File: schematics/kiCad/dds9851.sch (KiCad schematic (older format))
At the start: 8 parts, among them J1 PJ-102A, U1 Teensy-LC, U2 HC06

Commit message: new schematic
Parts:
- removed J1: PJ-102A, dmcginnis427:DC21Jack, symbol blinky-lite-basic-rescue:PJ-102A-dk_Barrel-Power-Connectors
- added TP-5V1, TP-GND1: TestPoint, Connector_PinHeader_2.54mm:PinHeader_1x01_P2.54mm_Vertical, symbol Connector:TestPoint
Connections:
- wire segments 31 -> 26
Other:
- moved on the sheet: C1
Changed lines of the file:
@@
 EESchema Schematic File Version 4
-LIBS:blinky-lite-basic-cache
 EELAYER 30 0
 EELAYER END
@@
 L power:GND #PWR010
 U 1 1 5E09DD5B
-P 10150 2100
-F 0 "#PWR010" H 10150 1850 50  0001 C CNN
-F 1 "GND" V 10155 1972 50  0000 R CNN
-F 2 "" H 10150 2100 50  0001 C CNN
-F 3 "" H 10150 2100 50  0001 C CNN
-	1    10150 2100
+P 10300 2200
+F 0 "#PWR010" H 10300 1950 50  0001 C CNN
+F 1 "GND" V 10305 2072 50  0000 R CNN
+F 2 "" H 10300 2200 50  0001 C CNN
+F 3 "" H 10300 2200 50  0001 C CNN
+	1    10300 2200
 	0    -1   -1   0
 $EndComp
@@
 L power:PWR_FLAG #FLG03
 U 1 1 5E13850E
-P 10000 2200
-F 0 "#FLG03" H 10000 2275 50  0001 C CNN
-F 1 "PWR_FLAG" H 10000 2373 50  0000 C CNN
-F 2 "" H 10000 2200 50  0001 C CNN
-F 3 "~" H 10000 2200 50  0001 C CNN
-	1    10000 2200
-	-1   0    0    1
-$EndComp
-Wire Wire Line
-	10000 2200 10000 2100
-Wire Wire Line
-	10000 2100 10150 2100
+P 9450 2300
+F 0 "#FLG03" H 9450 2375 50  0001 C CNN
+F 1 "PWR_FLAG" H 9450 2473 50  0000 C CNN
+F 2 "" H 9450 2300 50  0001 C CNN
+F 3 "~" H 9450 2300 50  0001 C CNN
+	1    9450 2300
+	-1   0    0    1
+$EndComp
+Wire Wire Line
+	9450 2300 9450 2200
 Wire Wire Line
 	10000 1800 10000 1900
 Wire Wire Line
 	10000 1900 10200 1900
-Connection ~ 10000 1900
-Connection ~ 10000 2100
 Wire Wire Line
 	10200 1250 10200 1900
@@
 L Device:C C1
 U 1 1 5E0B2B99
-P 9600 1350
-F 0 "C1" V 9348 1350 50  0000 C CNN
-F 1 "1uF" V 9439 1350 50  0000 C CNN
-F 2 "Capacitor_SMD:C_1206_3216Metric_Pad1.42x1.75mm_HandSolder" H 9638 1200 50  0001 C CNN
-F 3 "~" H 9600 1350 50  0001 C CNN
-	1    9600 1350
-	0    1    1    0
-$EndComp
-Wire Wire Line
-	9450 1350 9450 1900
-Wire Wire Line
-	9450 1900 10000 1900
-Wire Wire Line
-	9750 1350 9750 2100
-Wire Wire Line
-	9750 2100 10000 2100
+P 9450 2050
+F 0 "C1" V 9198 2050 50  0000 C CNN
+F 1 "1uF" V 9289 2050 50  0000 C CNN
+F 2 "Capacitor_SMD:C_1206_3216Metric_Pad1.42x1.75mm_HandSolder" H 9488 1900 50  0001 C CNN
+F 3 "~" H 9450 2050 50  0001 C CNN
+	1    9450 2050
+	-1   0    0    1
+$EndComp
 $Comp
 L power:GND #PWR017
@@
 NoConn ~ 6800 4050
 NoConn ~ 6800 4150
-NoConn ~ 4450 4250
 NoConn ~ 4450 4150
 NoConn ~ 4450 4050
@@
 Wire Wire Line
 	4000 2350 3800 2350
-Wire Wire Line
-	4050 2650 4450 2650
-$Comp
-L blinky-lite-basic-rescue:PJ-102A-dk_Barrel-Power-Connectors J1
-U 1 1 5E3829F9
-P 9450 850
-F 0 "J1" V 9337 606 50  0000 R CNN
-F 1 "PJ-102A" V 9428 606 50  0000 R CNN
-F 2 "dmcginnis427:DC21Jack" H 9650 1050 60  0001 L CNN
-F 3 "" H 9650 1150 60  0001 L CNN
-F 4 "" H 9650 1250 60  0001 L CNN "Digi-Key_PN"
-F 5 "" H 9650 1350 60  0001 L CNN "MPN"
-F 6 "" H 9650 1450 60  0001 L CNN "Category"
-F 7 "" H 9650 1550 60  0001 L CNN "Family"
-F 8 "" H 9650 1650 60  0001 L CNN "DK_Datasheet_Link"
-F 9 "" H 9650 1750 60  0001 L CNN "DK_Detail_Page"
-F 10 "" H 9650 1850 60  0001 L CNN "Description"
-F 11 "" H 9650 1950 60  0001 L CNN "Manufacturer"
-F 12 "" H 9650 2050 60  0001 L CNN "Status"
-	1    9450 850
-	0    -1   1    0
-$EndComp
-Wire Wire Line
-	9450 950  9450 1350
-Connection ~ 9450 1350
-Wire Wire Line
-	9650 950  9750 950
-Wire Wire Line
-	9750 950  9750 1350
-Connection ~ 9750 1350
-Wire Wire Line
-	9550 950  9650 950
-Connection ~ 9650 950
 $Comp
 L teensy:Teensy-LC U1
@@
 	1    0    0    -1
 $EndComp
-Wire Wire Line
-	4050 3150 4050 2650
-Wire Wire Line
-	3450 3150 4050 3150
-Wire Wire Line
-	3150 3150 3100 3150
-Wire Wire Line
-	2800 3150 2700 3150
-$Comp
-L Device:LED D2
-U 1 1 5E10E10F
-P 3300 3150
-F 0 "D2" H 3293 2895 50  0000 C CNN
-F 1 "LED" H 3293 2986 50  0000 C CNN
-F 2 "LED_THT:LED_D5.0mm" H 3300 3150 50  0001 C CNN
-F 3 "~" H 3300 3150 50  0001 C CNN
-	1    3300 3150
-	1    0    0    -1
-$EndComp
-$Comp
-L Device:R R2
-U 1 1 5E10E0FC
-P 2950 3150
-F 0 "R2" V 2743 3150 50  0000 C CNN
-F 1 "220" V 2834 3150 50  0000 C CNN
-F 2 "Resistor_SMD:R_1206_3216Metric_Pad1.42x1.75mm_HandSolder" V 2880 3150 50  0001 C CNN
-F 3 "~" H 2950 3150 50  0001 C CNN
-	1    2950 3150
-	0    -1   -1   0
-$EndComp
-$Comp
-L power:GND #PWR013
-U 1 1 5E10E108
-P 2700 3150
-F 0 "#PWR013" H 2700 2900 50  0001 C CNN
-F 1 "GND" V 2705 3022 50  0000 R CNN
-F 2 "" H 2700 3150 50  0001 C CNN
-F 3 "" H 2700 3150 50  0001 C CNN
-	1    2700 3150
-	0    1    1    0
-$EndComp
 NoConn ~ 6800 4250
 NoConn ~ 4450 3550
@@
 NoConn ~ 4450 2850
 NoConn ~ 4450 2750
+Wire Wire Line
+	3150 4250 3100 4250
+Wire Wire Line
+	2800 4250 2700 4250
+$Comp
+L Device:LED D2
+U 1 1 5E56B921
+P 3300 4250
+F 0 "D2" H 3293 3995 50  0000 C CNN
+F 1 "LED" H 3293 4086 50  0000 C CNN
+F 2 "LED_THT:LED_D5.0mm" H 3300 4250 50  0001 C CNN
+F 3 "~" H 3300 4250 50  0001 C CNN
+	1    3300 4250
+	1    0    0    -1
+$EndComp
+$Comp
+L Device:R R2
+U 1 1 5E56B927
+P 2950 4250
+F 0 "R2" V 2743 4250 50  0000 C CNN
+F 1 "220" V 2834 4250 50  0000 C CNN
+F 2 "Resistor_SMD:R_1206_3216Metric_Pad1.42x1.75mm_HandSolder" V 2880 4250 50  0001 C CNN
+F 3 "~" H 2950 4250 50  0001 C CNN
+	1    2950 4250
+	0    -1   -1   0
+$EndComp
+$Comp
+L power:GND #PWR05
+U 1 1 5E56B92D
+P 2700 4250
+F 0 "#PWR05" H 2700 4000 50  0001 C CNN
+F 1 "GND" V 2705 4122 50  0000 R CNN
+F 2 "" H 2700 4250 50  0001 C CNN
+F 3 "" H 2700 4250 50  0001 C CNN
+	1    2700 4250
+	0    1    1    0
+$EndComp
+Wire Wire Line
+	3450 4250 4450 4250
+NoConn ~ 4450 2650
+Wire Wire Line
+	10300 2200 9450 2200
+Connection ~ 9450 2200
+Wire Wire Line
+	10000 1900 9450 1900
+Connection ~ 10000 1900
+$Comp
+L Connector:TestPoint TP-5V1
+U 1 1 5F51E042
+P 8750 1850
+F 0 "TP-5V1" H 8808 1968 50  0000 L CNN
+F 1 "TestPoint" H 8808 1877 50  0000 L CNN
+F 2 "Connector_PinHeader_2.54mm:PinHeader_1x01_P2.54mm_Vertical" H 8950 1850 50  0001 C CNN
+F 3 "~" H 8950 1850 50  0001 C CNN
+	1    8750 1850
+	1    0    0    -1
+$EndComp
+$Comp
+L Connector:TestPoint TP-GND1
+U 1 1 5F51E6D9
+P 8750 2250
+F 0 "TP-GND1" H 8692 2276 50  0000 R CNN
+F 1 "TestPoint" H 8692 2367 50  0000 R CNN
+F 2 "Connector_PinHeader_2.54mm:PinHeader_1x01_P2.54mm_Vertical" H 8950 2250 50  0001 C CNN
+F 3 "~" H 8950 2250 50  0001 C CNN
+	1    8750 2250
+	-1   0    0    1
+$EndComp
+Wire Wire Line
+	9450 2200 8750 2200
+Wire Wire Line
+	8750 2200 8750 2250
+Wire Wire Line
+	9450 1900 8750 1900
+Wire Wire Line
+	8750 1900 8750 1850
+Connection ~ 9450 1900
 $EndSCHEMATC

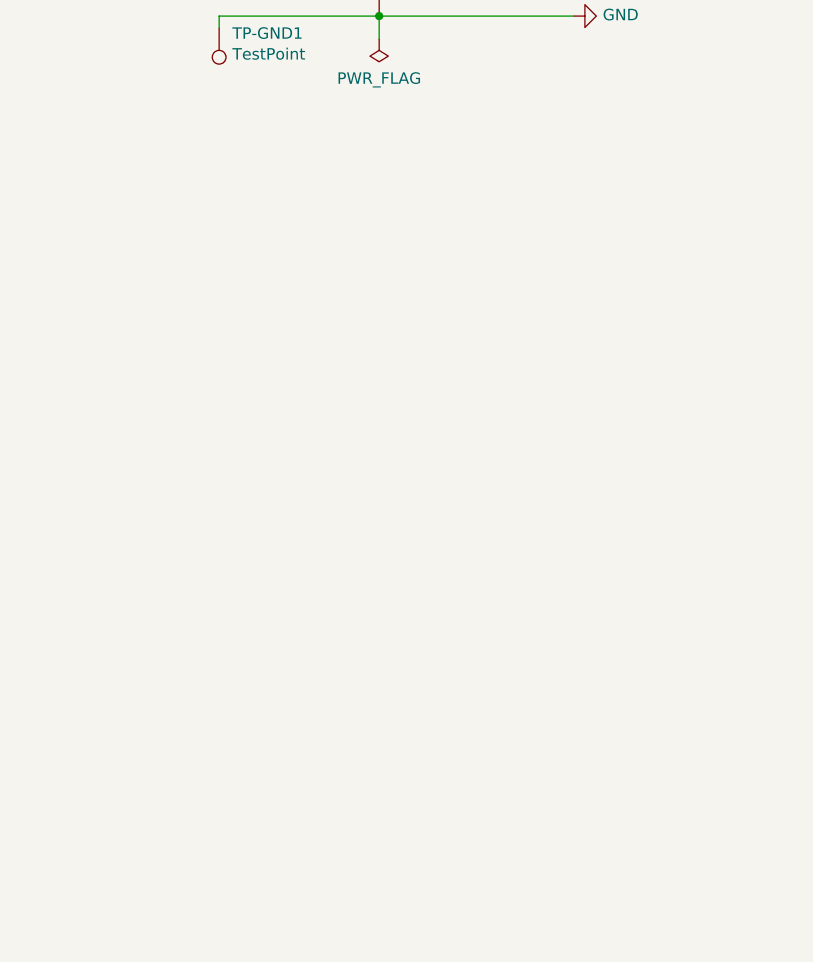
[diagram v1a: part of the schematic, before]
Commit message: added 9851 LTC, and MCP libraries
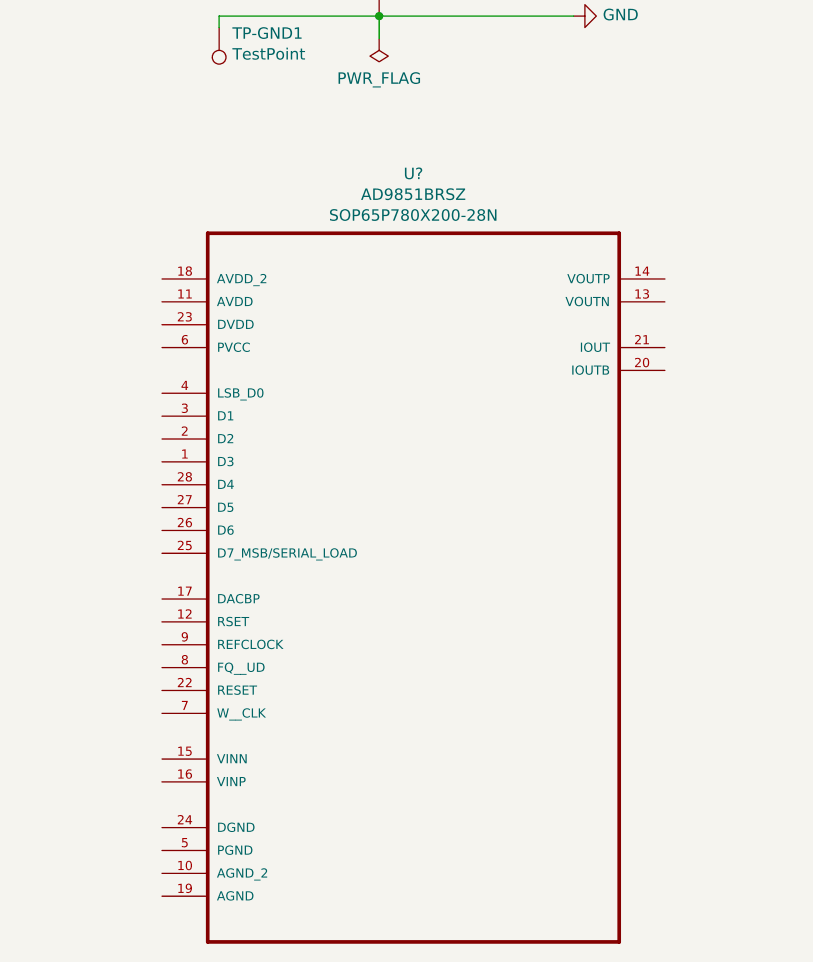
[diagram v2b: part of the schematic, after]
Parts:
- added U?: AD9851BRSZ, SOP65P780X200-28N, symbol ad9851:AD9851BRSZ
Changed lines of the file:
@@
 	8750 1900 8750 1850
 Connection ~ 9450 1900
+$Comp
+L ad9851:AD9851BRSZ U?
+U 1 1 5F7C104F
+P 9600 4550
+F 0 "U?" H 9600 6210 50  0000 C CNN
+F 1 "AD9851BRSZ" H 9600 6119 50  0000 C CNN
+F 2 "SOP65P780X200-28N" H 9600 6028 50  0000 C CNN
+F 3 "ANALOG DEVICES" H 9600 4550 50  0001 L BNN
+F 4 "-" H 9600 4550 50  0001 L BNN "Field4"
+F 5 "AD9851BRSZ" H 9600 4550 50  0001 L BNN "Field5"
+F 6 "19M8949" H 9600 4550 50  0001 L BNN "Field6"
+F 7 "SSOP-28" H 9600 4550 50  0001 L BNN "Field7"
+	1    9600 4550
+	1    0    0    -1
+$EndComp
 $EndSCHEMATC

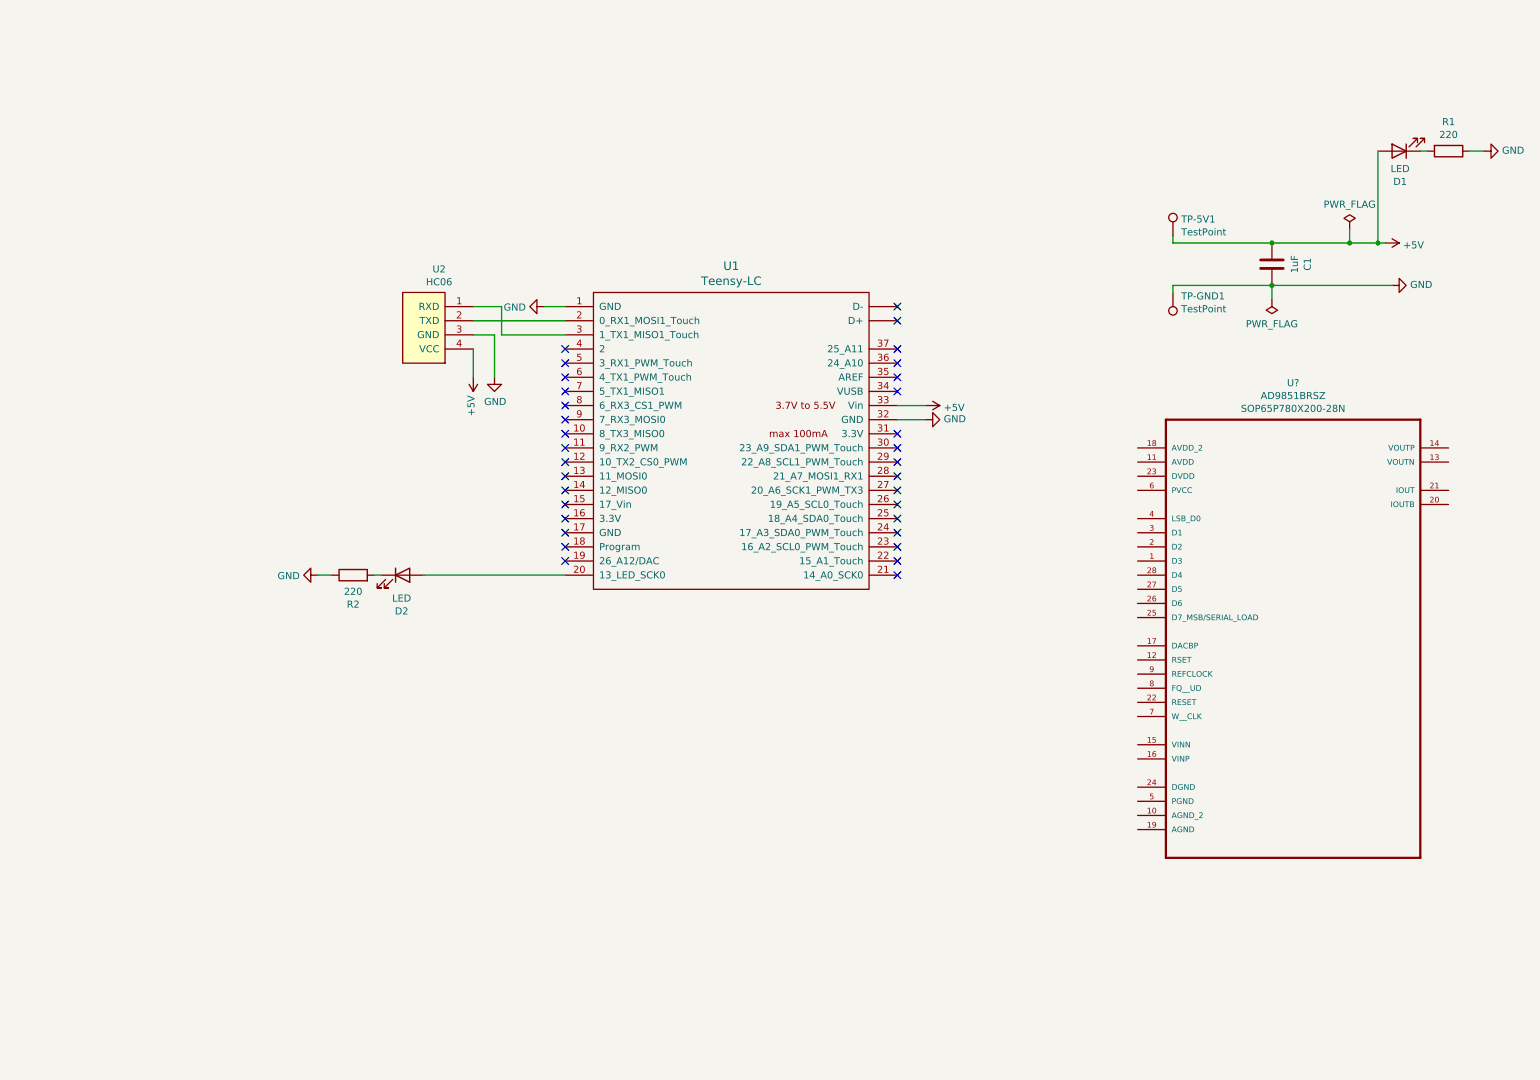
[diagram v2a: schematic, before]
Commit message: schematic done - working on pcb
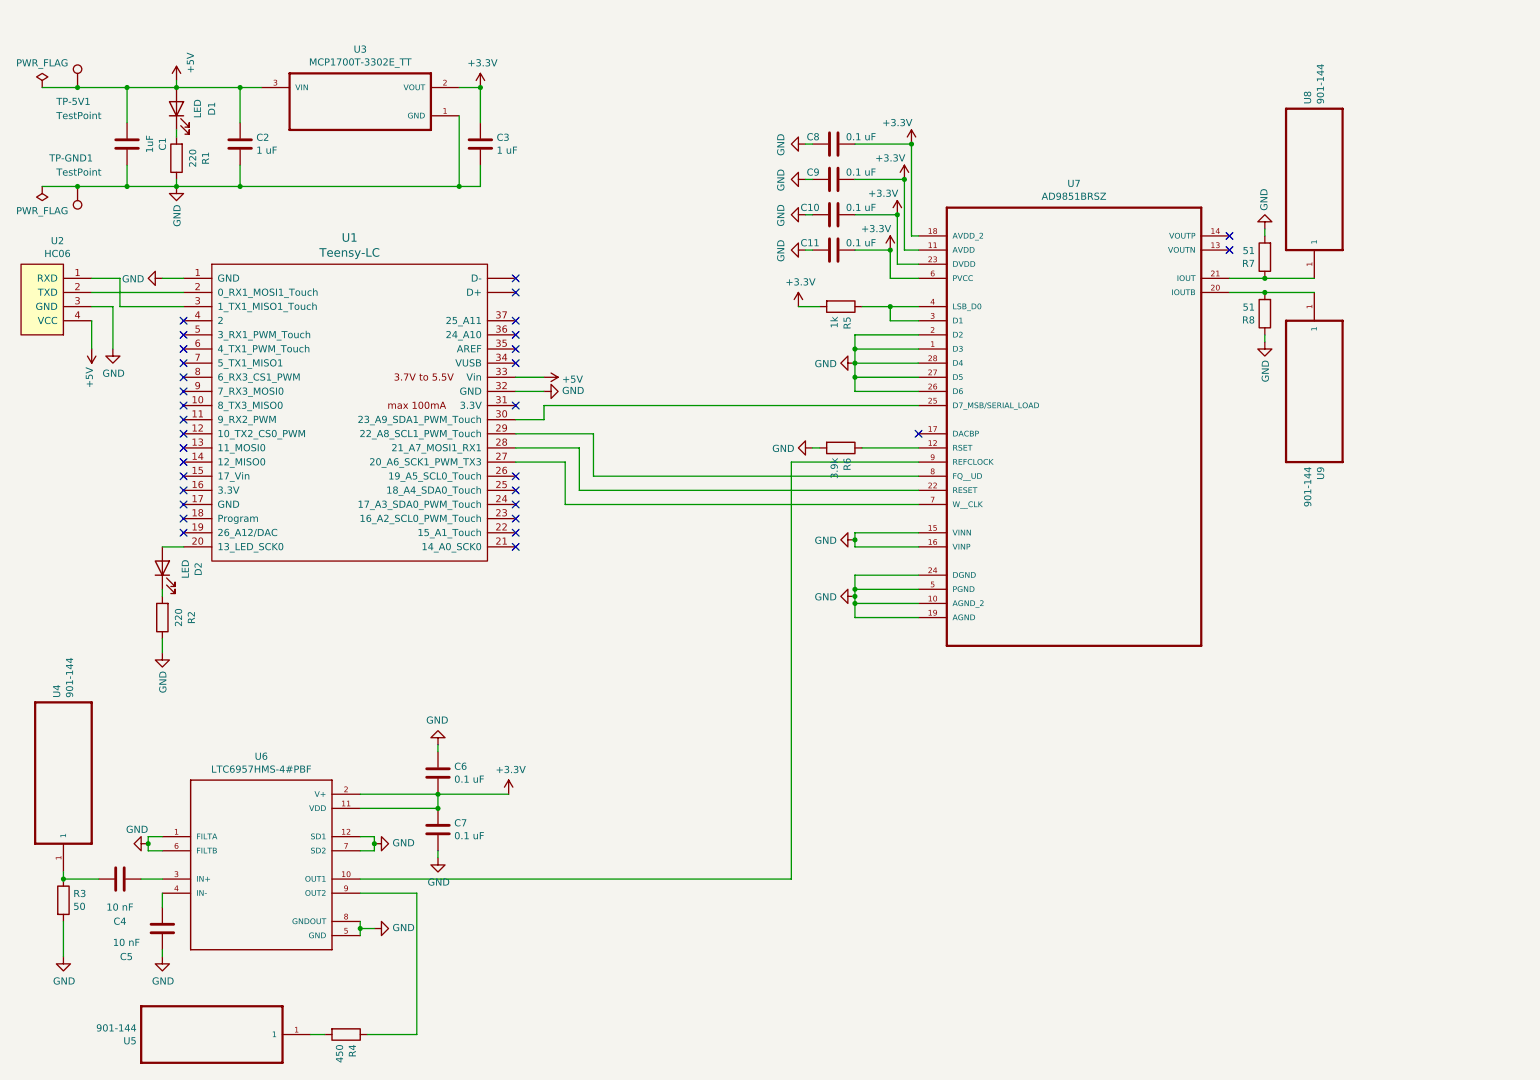
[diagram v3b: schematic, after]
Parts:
- removed U?: AD9851BRSZ, SOP65P780X200-28N, symbol ad9851:AD9851BRSZ
- added C10, C11, C6, C7, C8, C9: 0.1 uF, Capacitor_SMD:C_1206_3216Metric_Pad1.42x1.75mm_HandSolder, symbol Device:C
- added C2, C3: 1 uF, Capacitor_SMD:C_1206_3216Metric_Pad1.42x1.75mm_HandSolder, symbol Device:C
- added C4, C5: 10 nF, Capacitor_SMD:C_1206_3216Metric_Pad1.42x1.75mm_HandSolder, symbol Device:C
- added R3: 50, Resistor_SMD:R_1206_3216Metric_Pad1.42x1.75mm_HandSolder, symbol Device:R
- added R4: 450, Resistor_SMD:R_1206_3216Metric_Pad1.42x1.75mm_HandSolder, symbol Device:R
- added R5: 1k, Resistor_SMD:R_1206_3216Metric_Pad1.42x1.75mm_HandSolder, symbol Device:R
- added R6: 3.9k, Resistor_SMD:R_1206_3216Metric_Pad1.42x1.75mm_HandSolder, symbol Device:R
- added R7, R8: 51, Resistor_SMD:R_1206_3216Metric_Pad1.42x1.75mm_HandSolder, symbol Device:R
- added U3: MCP1700T-3302E_TT, MCP1700T:SOT95P237X112-3N, symbol MCP1700:MCP1700T-3302E_TT
- added U4, U5, U8, U9: 901-144, SMA_Female:SMA_Female, symbol SMA_Female:901-144
- added U6: LTC6957HMS-4#PBF, LTC6957:SOP65P490X110-12N, symbol LTC6957:LTC6957HMS-4#PBF
- added U7: AD9851BRSZ, AD9851:SOP65P780X200-28N, symbol ad9851:AD9851BRSZ
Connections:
- net +5V: now also C2.1, U3.3 (VIN)
- net GND: now also C10.1, C11.1, C2.2, C3.2, C5.2, C6.1, C7.2, C8.1, C9.1, R3.2, R6.2, R7.2, R8.1, U3.1 (GND), U6.1 (FILTA), U6.12 (SD1), U6.5 (GND), U6.6 (FILTB), U6.7 (SD2), U6.8 (GNDOUT), U7.1 (D3), U7.10 (AGND_2), U7.15 (VINN), U7.16 (VINP), U7.19 (AGND), U7.2 (D2), U7.24 (DGND), U7.26 (D6), U7.27 (D5), U7.28 (D4), U7.5 (PGND)
- net at U1.27 (20_A6_SCK1_PWM_TX3): now also U7.7 (W__CLK)
- net at U1.28 (21_A7_MOSI1_RX1): now also U7.22 (RESET)
- net at U1.29 (22_A8_SCL1_PWM_Touch): now also U7.8 (FQ__UD)
- net at U1.30 (23_A9_SDA1_PWM_Touch): now also U7.25 (D7_MSB/SERIAL_LOAD)
- new net: C4.2, R3.1, U4.1
- new net: R4.2, U5.1
- new net: R4.1, U6.9 (OUT2)
- new net: R6.1, U7.12 (RSET)
- new net: R8.2, U7.20 (IOUTB), U9.1
- new net: R7.1, U7.21 (IOUT), U8.1
- new net: R5.1, U7.3 (D1), U7.4 (LSB_D0)
- new net: U6.10 (OUT1), U7.9 (REFCLOCK)
- new net: C4.1, U6.3 (IN+)
- new net: C5.1, U6.4 (IN-)
- new net +3V3: C10.2, C11.2, C3.1, C6.2, C7.1, C8.2, C9.2, R5.2, U3.2 (VOUT), U6.11 (VDD), U6.2 (V+), U7.11 (AVDD), U7.18 (AVDD_2), U7.23 (DVDD), U7.6 (PVCC)
- no-connect marks 33 -> 32
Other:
- moved on the sheet: C1, D1, D2, R1, R2, TP-5V1, TP-GND1, U1, U2

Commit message: components placed
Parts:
- removed C1: 1uF, Capacitor_SMD:C_1206_3216Metric_Pad1.42x1.75mm_HandSolder, symbol Device:C
- removed C11, C6, C9: 0.1 uF, Capacitor_SMD:C_1206_3216Metric_Pad1.42x1.75mm_HandSolder, symbol Device:C
- renumbered C4 to C1, C5 to C2, C2 to C3, C7 to C4, C3 to C5, C8 to C6, C10 to C8, D2 to D1, D1 to D2, R3 to R1, R1 to R3, U4 to U1, U5 to U3, U6 to U4, U1 to U5, U3 to U6
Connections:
- net at R4.1: now also U4.10 (OUT1); no longer U4.9 (OUT2)
- net at U7.9 (REFCLOCK): now also U4.9 (OUT2); no longer U4.10 (OUT1)
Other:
- moved on the sheet: C6, C8
